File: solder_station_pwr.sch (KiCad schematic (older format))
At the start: 47 parts, among them J1 PWR_MAIN_LINE, J2 FB, J3 Conn_01x04, J5 DESOLDER, J6 Conn_01x03, Q3 2SD669, T1 RingTrafo_40U, T2 220V-7V5, U1 TLC555, U2 L7805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

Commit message: add darligton stage instead of simple transitor
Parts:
- removed Q3: 2SD669, Package_TO_SOT_THT:TO-126-3_Vertical, symbol Device:Q_NPN_EBC
- added Q1: 2N7002, Package_TO_SOT_SMD:SOT-23_Handsoldering, symbol Device:Q_NMOS_GSD
- added Q3: 2SD669, Package_TO_SOT_THT:TO-126-3_Vertical, symbol Device:Q_NPN_ECB
- C14: value 10n -> 4n7
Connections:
- net labels removed: 7V5P
- wire segments 171 -> 176
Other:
- moved on the sheet: D2, J2, J3, J6, T1
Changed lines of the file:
@@
 EESchema Schematic File Version 4
 LIBS:solder_station_pwr-cache
-EELAYER 26 0
+EELAYER 28 0
 EELAYER END
 $Descr A4 11693 8268
@@
 	8450 3050 8950 3050
 Connection ~ 8950 3050
-Text Label 7550 2250 2    50   ~ 0
-7V5P
 $Comp
 L Regulator_Linear:L7805 U2
@@
 L Device:D_Schottky D2
 U 1 1 5B55017E
-P 4050 6300
-F 0 "D2" H 4050 6200 50  0000 C CNN
-F 1 "SD103BW" H 4050 6400 50  0000 C CNN
-F 2 "Diode_SMD:D_SOD-123" H 4050 6300 50  0001 C CNN
-F 3 "~" H 4050 6300 50  0001 C CNN
-	1    4050 6300
+P 4750 6350
+F 0 "D2" H 4750 6250 50  0000 C CNN
+F 1 "SD103BW" H 4750 6450 50  0000 C CNN
+F 2 "Diode_SMD:D_SOD-123" H 4750 6350 50  0001 C CNN
+F 3 "~" H 4750 6350 50  0001 C CNN
+	1    4750 6350
 	0    1    1    0
-$EndComp
-$Comp
-L Device:Q_NPN_EBC Q3
-U 1 1 5B55037E
-P 3600 6300
-F 0 "Q3" H 3450 6450 50  0000 L CNN
-F 1 "2SD669" V 3800 6150 50  0000 L CNN
-F 2 "Package_TO_SOT_THT:TO-126-3_Vertical" H 3800 6400 50  0001 C CNN
-F 3 "~" H 3600 6300 50  0001 C CNN
-	1    3600 6300
-	1    0    0    -1
 $EndComp
 $Comp
@@
 L Device:Transformer_1P_SS T1
 U 1 1 5B56D747
-P 4100 5450
-F 0 "T1" H 4100 5750 50  0000 C CNN
-F 1 "RingTrafo_40U" H 4100 5150 50  0000 C CNN
-F 2 "custom:Transformer_toroid_v_18mm" H 4100 5450 50  0001 C CNN
-F 3 "~" H 4100 5450 50  0001 C CNN
-	1    4100 5450
+P 4800 5450
+F 0 "T1" H 4800 5750 50  0000 C CNN
+F 1 "RingTrafo_40U" H 4800 5150 50  0000 C CNN
+F 2 "custom:Transformer_toroid_v_18mm" H 4800 5450 50  0001 C CNN
+F 3 "~" H 4800 5450 50  0001 C CNN
+	1    4800 5450
 	1    0    0    -1
 $EndComp
@@
 P 1400 6850
 F 0 "C14" H 1515 6896 50  0000 L CNN
-F 1 "10n" H 1515 6805 50  0000 L CNN
+F 1 "4n7" H 1515 6805 50  0000 L CNN
 F 2 "Capacitor_SMD:C_0805_2012Metric_Pad1.15x1.40mm_HandSolder" H 1438 6700 50  0001 C CNN
 F 3 "~" H 1400 6850 50  0001 C CNN
@@
 	3000 6300 2850 6300
 Wire Wire Line
-	3200 6300 3400 6300
-Wire Wire Line
-	3700 6500 3700 6600
-Wire Wire Line
-	3700 7150 2950 7150
-Connection ~ 2950 7150
-Wire Wire Line
-	3700 6600 4050 6600
-Wire Wire Line
-	4050 6600 4050 6450
-Connection ~ 3700 6600
-Wire Wire Line
-	3700 6600 3700 7150
-Wire Wire Line
-	4050 6150 4050 5950
-Wire Wire Line
-	4050 5950 3700 5950
-Wire Wire Line
-	3700 5950 3700 6100
-Wire Wire Line
-	3700 5650 3700 5950
-Connection ~ 3700 5950
-Wire Wire Line
-	3700 5250 3700 5050
-Wire Wire Line
-	3700 5050 2350 5050
+	4400 6750 4400 6850
+Wire Wire Line
+	4400 6850 4750 6850
+Connection ~ 4400 6850
+Wire Wire Line
+	4400 6850 4400 7150
+Wire Wire Line
+	4400 5250 4400 5050
 Connection ~ 2350 5050
 Wire Wire Line
 	2350 5050 2350 4750
-Connection ~ 3700 5050
 Wire Wire Line
 	1400 5650 1400 5050
@@
 	1400 6100 1850 6100
 Wire Wire Line
-	1400 5050 2350 5050
-Wire Wire Line
 	1400 6400 1850 6400
 Wire Wire Line
@@
 Wire Wire Line
 	3350 5800 3350 5950
-Text Label 5150 5550 0    50   ~ 0
-7V5P
-$Comp
-L Connector_Generic:Conn_01x03 J6
-U 1 1 5B54609A
-P 5600 5450
-F 0 "J6" H 5680 5492 50  0000 L CNN
-F 1 "Conn_01x03" H 5680 5401 50  0000 L CNN
-F 2 "Connector_PinSocket_2.54mm:PinSocket_1x03_P2.54mm_Vertical" H 5600 5450 50  0001 C CNN
-F 3 "~" H 5600 5450 50  0001 C CNN
-	1    5600 5450
-	1    0    0    -1
-$EndComp
-Wire Wire Line
-	5400 5550 5150 5550
-Wire Wire Line
-	5150 5350 5400 5350
 $Comp
 L power:+36V #PWR01
 U 1 1 5B5C145A
-P 4950 6850
-F 0 "#PWR01" H 4950 6700 50  0001 C CNN
-F 1 "+36V" H 4965 7023 50  0000 C CNN
-F 2 "" H 4950 6850 50  0001 C CNN
-F 3 "" H 4950 6850 50  0001 C CNN
-	1    4950 6850
+P 5950 6750
+F 0 "#PWR01" H 5950 6600 50  0001 C CNN
+F 1 "+36V" H 5965 6923 50  0000 C CNN
+F 2 "" H 5950 6750 50  0001 C CNN
+F 3 "" H 5950 6750 50  0001 C CNN
+	1    5950 6750
 	1    0    0    -1
 $EndComp
@@
 Text Label 1850 1500 0    50   ~ 0
 UNR_5V
-$Comp
-L Connector_Generic:Conn_01x02 J2
-U 1 1 5B60DB5B
-P 5200 6350
-F 0 "J2" H 5280 6342 50  0000 L CNN
-F 1 "FB" H 5280 6251 50  0000 L CNN
-F 2 "Connector_PinHeader_2.54mm:PinHeader_1x02_P2.54mm_Vertical" H 5200 6350 50  0001 C CNN
-F 3 "~" H 5200 6350 50  0001 C CNN
-	1    5200 6350
-	1    0    0    -1
-$EndComp
-Text Label 4850 5650 2    50   ~ 0
+Text Label 5250 5650 0    50   ~ 0
 FB1
-Text Label 4700 6450 0    50   ~ 0
-FB1
-Wire Wire Line
-	4700 6450 5000 6450
-Wire Wire Line
-	5000 6350 4700 6350
-Text Label 4850 5250 2    50   ~ 0
+Text Label 5250 5250 0    50   ~ 0
 FB2
-Text Label 4700 6350 0    50   ~ 0
-FB2
-Wire Wire Line
-	4500 5450 5400 5450
-Wire Wire Line
-	5150 5050 5150 5350
-Wire Wire Line
-	3700 5050 5150 5050
-Wire Wire Line
-	4850 5650 4500 5650
-Wire Wire Line
-	4500 5250 4850 5250
+Wire Wire Line
+	5200 5250 5550 5250
 $Comp
 L power:+5V #PWR0104
 U 1 1 5B64B6CC
-P 4750 6850
-F 0 "#PWR0104" H 4750 6700 50  0001 C CNN
-F 1 "+5V" H 4765 7023 50  0000 C CNN
-F 2 "" H 4750 6850 50  0001 C CNN
-F 3 "" H 4750 6850 50  0001 C CNN
-	1    4750 6850
+P 5750 6750
+F 0 "#PWR0104" H 5750 6600 50  0001 C CNN
+F 1 "+5V" H 5765 6923 50  0000 C CNN
+F 2 "" H 5750 6750 50  0001 C CNN
+F 3 "" H 5750 6750 50  0001 C CNN
+	1    5750 6750
 	1    0    0    -1
 $EndComp
@@
 L power:-5V #PWR0105
 U 1 1 5B64B913
-P 4750 7500
-F 0 "#PWR0105" H 4750 7600 50  0001 C CNN
-F 1 "-5V" H 4765 7673 50  0000 C CNN
-F 2 "" H 4750 7500 50  0001 C CNN
-F 3 "" H 4750 7500 50  0001 C CNN
-	1    4750 7500
+P 5750 7400
+F 0 "#PWR0105" H 5750 7500 50  0001 C CNN
+F 1 "-5V" H 5765 7573 50  0000 C CNN
+F 2 "" H 5750 7400 50  0001 C CNN
+F 3 "" H 5750 7400 50  0001 C CNN
+	1    5750 7400
 	-1   0    0    1
 $EndComp
@@
 L power:GND #PWR0106
 U 1 1 5B64BA52
-P 4500 7500
-F 0 "#PWR0106" H 4500 7250 50  0001 C CNN
-F 1 "GND" H 4505 7327 50  0000 C CNN
-F 2 "" H 4500 7500 50  0001 C CNN
-F 3 "" H 4500 7500 50  0001 C CNN
-	1    4500 7500
-	1    0    0    -1
-$EndComp
-Wire Wire Line
-	4500 7500 4500 7100
-Wire Wire Line
-	4500 7100 5000 7100
-Wire Wire Line
-	4750 6850 4750 7000
-Wire Wire Line
-	4750 7000 5000 7000
-Wire Wire Line
-	5000 7200 4750 7200
-Wire Wire Line
-	4750 7200 4750 7500
+P 5500 7400
+F 0 "#PWR0106" H 5500 7150 50  0001 C CNN
+F 1 "GND" H 5505 7227 50  0000 C CNN
+F 2 "" H 5500 7400 50  0001 C CNN
+F 3 "" H 5500 7400 50  0001 C CNN
+	1    5500 7400
+	1    0    0    -1
+$EndComp
+Wire Wire Line
+	5500 7400 5500 7000
+Wire Wire Line
+	5500 7000 6000 7000
+Wire Wire Line
+	5750 6750 5750 6900
+Wire Wire Line
+	5750 6900 6000 6900
+Wire Wire Line
+	6000 7100 5750 7100
+Wire Wire Line
+	5750 7100 5750 7400
 $Comp
 L Connector_Generic:Conn_01x04 J3
 U 1 1 5B66CCE5
-P 5200 7100
-F 0 "J3" H 5280 7092 50  0000 L CNN
-F 1 "Conn_01x04" H 5280 7001 50  0000 L CNN
-F 2 "Connector_PinSocket_2.54mm:PinSocket_1x04_P2.54mm_Vertical" H 5200 7100 50  0001 C CNN
-F 3 "~" H 5200 7100 50  0001 C CNN
-	1    5200 7100
-	1    0    0    -1
-$EndComp
-Wire Wire Line
-	4950 6850 4950 7300
-Wire Wire Line
-	4950 7300 5000 7300
+P 6200 7000
+F 0 "J3" H 6280 6992 50  0000 L CNN
+F 1 "Conn_01x04" H 6280 6901 50  0000 L CNN
+F 2 "Connector_PinSocket_2.54mm:PinSocket_1x04_P2.54mm_Vertical" H 6200 7000 50  0001 C CNN
+F 3 "~" H 6200 7000 50  0001 C CNN
+	1    6200 7000
+	1    0    0    -1
+$EndComp
+Wire Wire Line
+	5950 6750 5950 7200
+Wire Wire Line
+	5950 7200 6000 7200
 $Comp
 L power:+36V #PWR0107
@@
 	1300 850  1300 1250
 Connection ~ 1300 1250
+$Comp
+L Device:Q_NPN_ECB Q3
+U 1 1 5BC3B0FA
+P 4300 6550
+F 0 "Q3" H 4250 6700 50  0000 L CNN
+F 1 "2SD669" H 4100 6350 50  0000 L CNN
+F 2 "Package_TO_SOT_THT:TO-126-3_Vertical" H 4500 6650 50  0001 C CNN
+F 3 "~" H 4300 6550 50  0001 C CNN
+	1    4300 6550
+	1    0    0    -1
+$EndComp
+$Comp
+L Device:Q_NMOS_GSD Q1
+U 1 1 5BC54008
+P 3800 6300
+F 0 "Q1" H 4006 6346 50  0000 L CNN
+F 1 "2N7002" H 4006 6255 50  0000 L CNN
+F 2 "Package_TO_SOT_SMD:SOT-23_Handsoldering" H 4000 6400 50  0001 C CNN
+F 3 "~" H 3800 6300 50  0001 C CNN
+	1    3800 6300
+	1    0    0    -1
+$EndComp
+Wire Wire Line
+	5200 5450 5450 5450
+Wire Wire Line
+	3200 6300 3600 6300
+Wire Wire Line
+	4400 5900 3900 5900
+Wire Wire Line
+	3900 5900 3900 6100
+Wire Wire Line
+	4400 5900 4750 5900
+Connection ~ 4400 5900
+Wire Wire Line
+	4750 5900 4750 6200
+Wire Wire Line
+	4400 5900 4400 6350
+Wire Wire Line
+	4750 6500 4750 6850
+Wire Wire Line
+	2950 7150 4400 7150
+Connection ~ 2950 7150
+Wire Wire Line
+	4100 6550 3900 6550
+Wire Wire Line
+	3900 6550 3900 6500
+Wire Wire Line
+	2350 5050 1400 5050
+Wire Wire Line
+	4400 5900 4400 5650
+$Comp
+L Connector_Generic:Conn_01x02 J2
+U 1 1 5B60DB5B
+P 5850 5550
+F 0 "J2" H 5930 5542 50  0000 L CNN
+F 1 "FB" H 5930 5451 50  0000 L CNN
+F 2 "Connector_PinHeader_2.54mm:PinHeader_1x02_P2.54mm_Vertical" H 5850 5550 50  0001 C CNN
+F 3 "~" H 5850 5550 50  0001 C CNN
+	1    5850 5550
+	1    0    0    -1
+$EndComp
+Wire Wire Line
+	4400 5050 5450 5050
+$Comp
+L Connector_Generic:Conn_01x03 J6
+U 1 1 5B54609A
+P 3550 5050
+F 0 "J6" H 3630 5092 50  0000 L CNN
+F 1 "Conn_01x03" H 3630 5001 50  0000 L CNN
+F 2 "Connector_PinSocket_2.54mm:PinSocket_1x03_P2.54mm_Vertical" H 3550 5050 50  0001 C CNN
+F 3 "~" H 3550 5050 50  0001 C CNN
+	1    3550 5050
+	-1   0    0    -1
+$EndComp
+Wire Wire Line
+	5450 5450 5450 5050
+Wire Wire Line
+	5200 5650 5650 5650
+Wire Wire Line
+	5550 5250 5550 5550
+Wire Wire Line
+	5550 5550 5650 5550
+$Comp
+L power:+5V #PWR02
+U 1 1 5BE33567
+P 4400 4700
+F 0 "#PWR02" H 4400 4550 50  0001 C CNN
+F 1 "+5V" H 4415 4873 50  0000 C CNN
+F 2 "" H 4400 4700 50  0001 C CNN
+F 3 "" H 4400 4700 50  0001 C CNN
+	1    4400 4700
+	-1   0    0    -1
+$EndComp
+Wire Wire Line
+	4400 4700 4400 4950
+Text Label 4100 5150 2    50   ~ 0
+UNR_5V
+Wire Wire Line
+	3750 5150 4100 5150
+Wire Wire Line
+	3750 5050 4400 5050
+Connection ~ 4400 5050
+Wire Wire Line
+	3750 4950 4400 4950
 $EndSCHEMATC

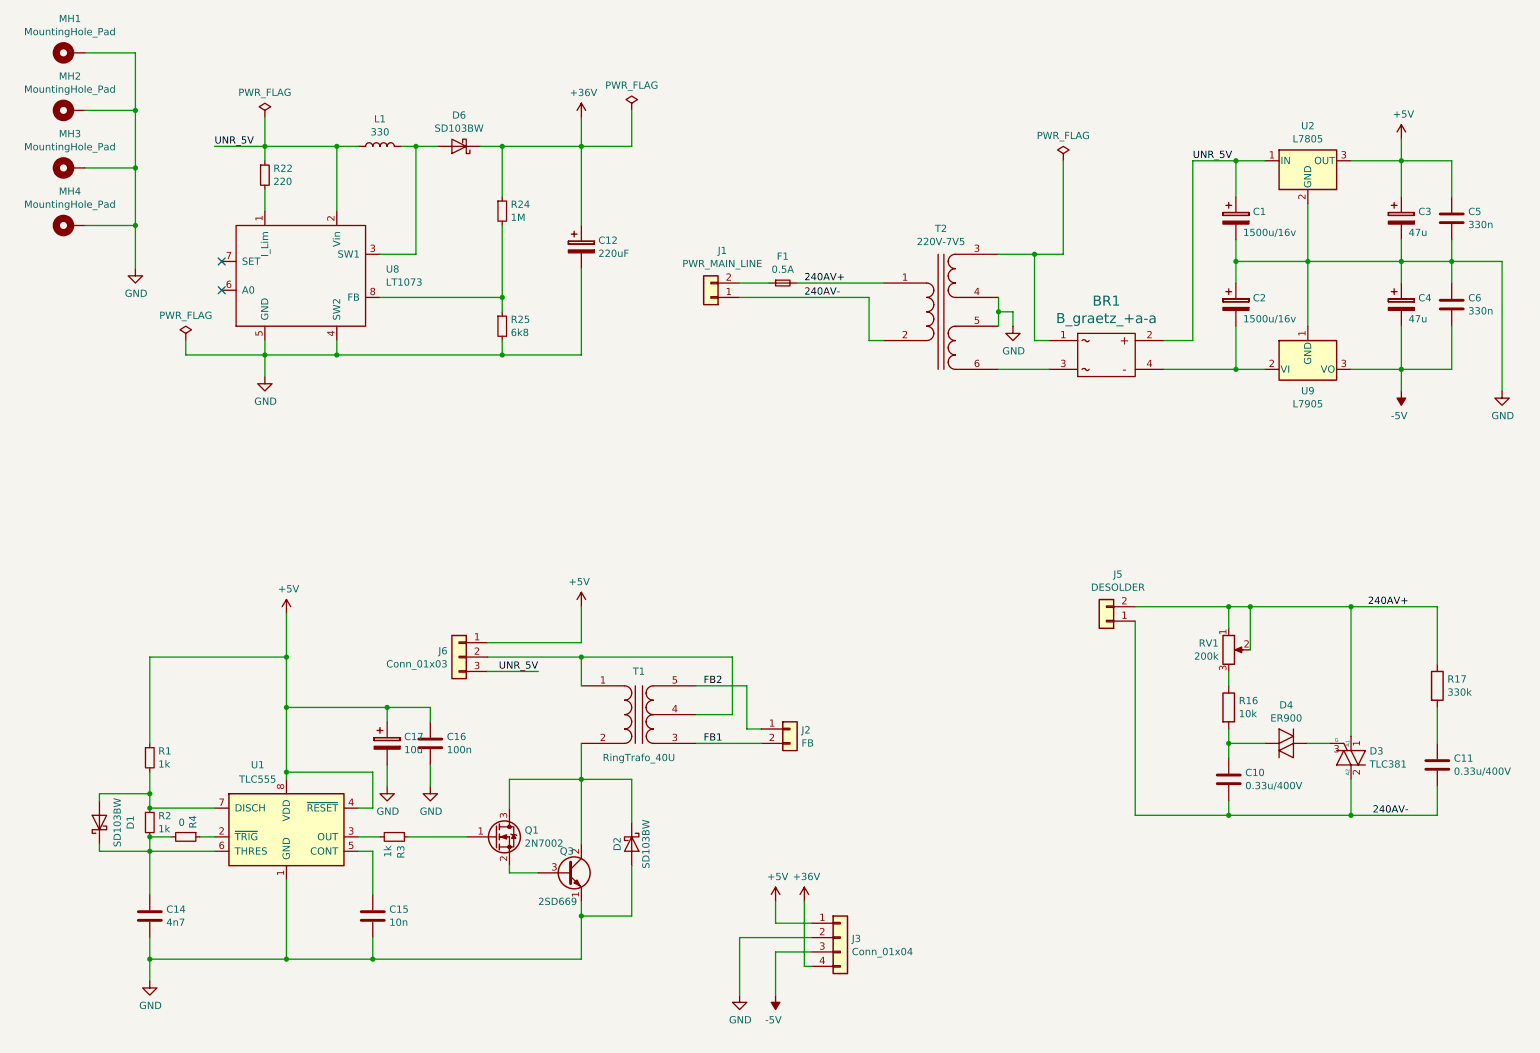
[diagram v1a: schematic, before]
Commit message: remove ne555, using the atmega pwm OC0B to control the transistor
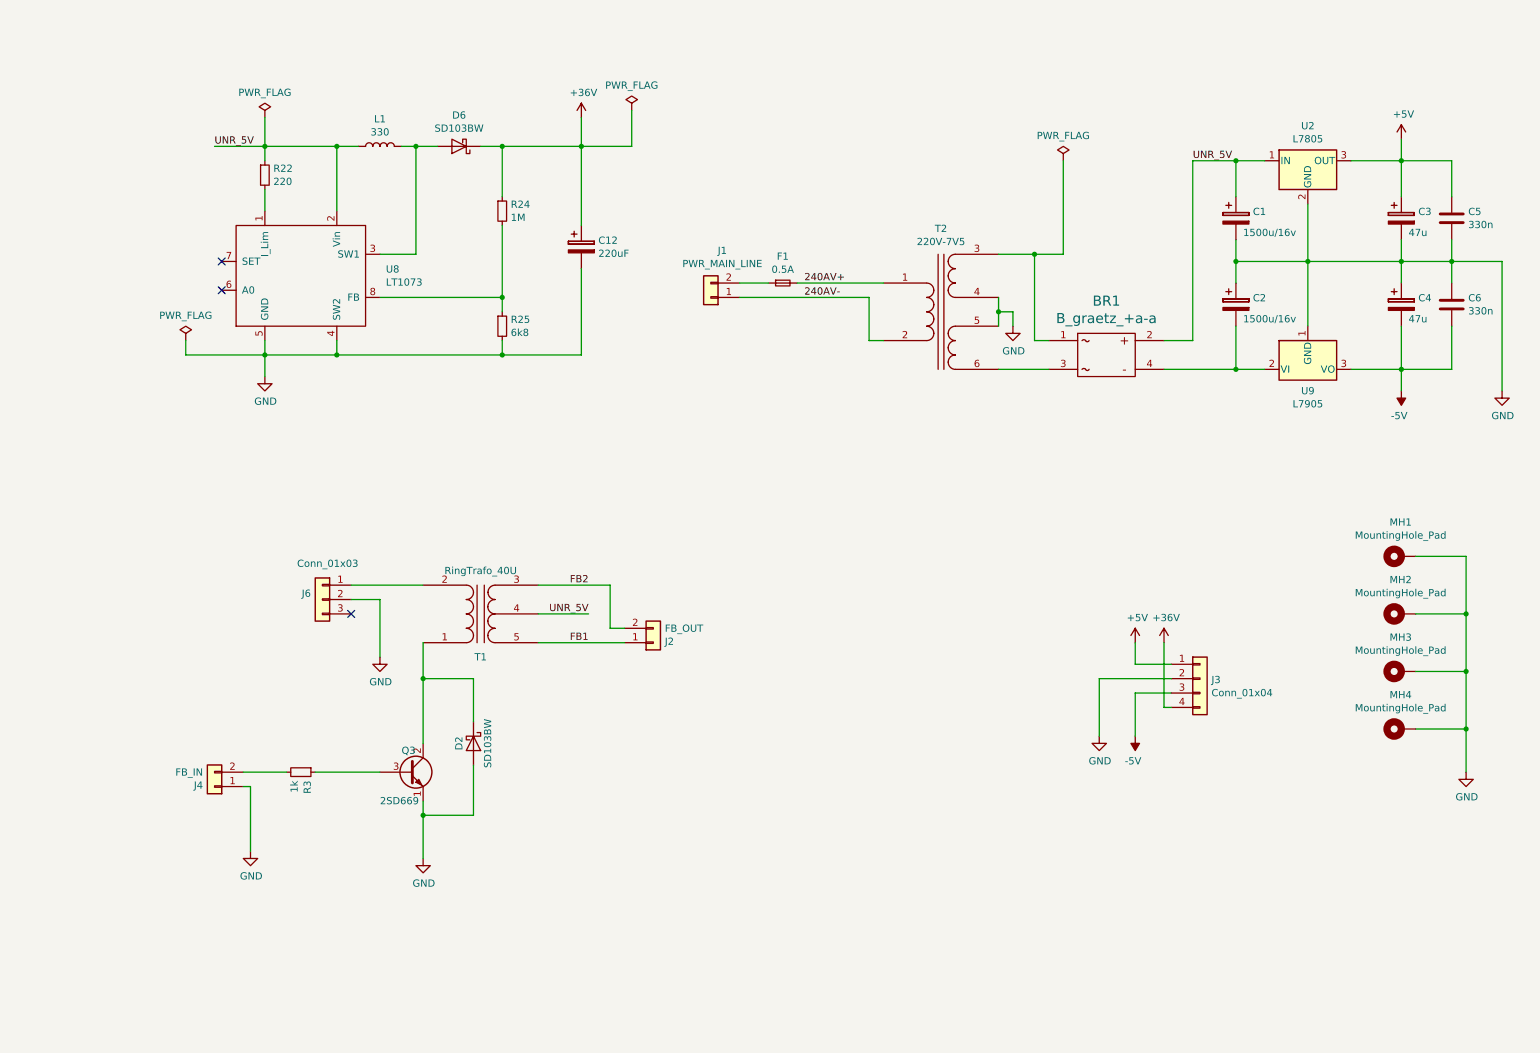
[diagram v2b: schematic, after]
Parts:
- removed C10, C11: 0.33u/400V, Capacitor_THT:C_Rect_L19.0mm_W8.0mm_P15.00mm_MKS4, symbol Device:C
- removed C14: 4n7, Capacitor_SMD:C_0805_2012Metric_Pad1.15x1.40mm_HandSolder, symbol Device:C
- removed C15: 10n, Capacitor_SMD:C_0805_2012Metric_Pad1.15x1.40mm_HandSolder, symbol Device:C
- removed C16: 100n, Capacitor_SMD:C_0805_2012Metric_Pad1.15x1.40mm_HandSolder, symbol Device:C
- removed C17: 10u, Capacitor_Tantalum_SMD:CP_EIA-6032-15_Kemet-U_Pad2.25x2.35mm_HandSolder, symbol Device:CP
- removed D1: SD103BW, Diode_SMD:D_SOD-123, symbol Device:D_Schottky
- removed D3: TLC381, Package_TO_SOT_THT:TO-220-3_Vertical, symbol Device:Q_TRIAC_A1A2G
- removed D4: ER900, Diode_THT:D_A-405_P7.62mm_Horizontal, symbol Device:DIAC
- removed J5: DESOLDER, Connector_Wire:SolderWirePad_1x02_P5.08mm_Drill1.5mm, symbol Connector_Generic:Conn_01x02
- removed Q1: 2N7002, Package_TO_SOT_SMD:SOT-23_Handsoldering, symbol Device:Q_NMOS_GSD
- removed R1, R2: 1k, Resistor_SMD:R_0805_2012Metric_Pad1.15x1.40mm_HandSolder, symbol Device:R_Small
- removed R16: 10k, Resistor_THT:R_Axial_DIN0207_L6.3mm_D2.5mm_P10.16mm_Horizontal, symbol Device:R
- removed R17: 330k, Resistor_THT:R_Axial_DIN0207_L6.3mm_D2.5mm_P10.16mm_Horizontal, symbol Device:R
- removed R4: 0, Resistor_SMD:R_1206_3216Metric_Pad1.42x1.75mm_HandSolder, symbol Device:R_Small
- removed RV1: 200k, TerminalBlock_4Ucon:TerminalBlock_4Ucon_1x03_P3.50mm_Horizontal, symbol Device:R_POT
- removed U1: TLC555, Package_SO:SOIC-8_3.9x4.9mm_P1.27mm, symbol Timer:TLC555
- added J4: FB_IN, Connector_PinHeader_2.54mm:PinHeader_1x02_P2.54mm_Vertical, symbol Connector_Generic:Conn_01x02
- J2: value FB -> FB_OUT
- J6: footprint Connector_PinSocket_2.54mm:PinSocket_1x03_P2.54mm_Vertical -> Connector_PinSocket_2.54mm:PinSocket_1x03_P2.54mm_Vertical_SMD_Pin1Left
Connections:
- net +5V: no longer J6.1 (Pin_1)
- net FB1: now also J2.1 (Pin_1), T1.5 (SB); no longer J2.2 (Pin_2), T1.3 (SA)
- net FB2: now also J2.2 (Pin_2), T1.3 (SA); no longer J2.1 (Pin_1), T1.5 (SB)
- net GND: now also J6.2 (Pin_2), J4.1 (Pin_1)
- net UNR_5V: now also T1.4 (SC); no longer J6.3 (Pin_3)
- net at R3.2: now also J4.2 (Pin_2)
- net at D2.1 (K), Q3.2 (C): now also T1.1 (AA); no longer T1.2 (AB)
- net at R3.1: now also Q3.3 (B)
- new net: J6.1 (Pin_1), T1.2 (AB)
- no-connect marks 2 -> 3
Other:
- moved on the sheet: D2, J2, J3, J6, MH1, MH2, MH3, MH4, Q3, R3, T1

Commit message: Add power suppply has now just 2 differents 5 volt and a -5 volt
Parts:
- removed D2: SD103BW, Diode_SMD:D_SOD-123, symbol Device:D_Schottky
- removed J4: FB_IN, Connector_PinHeader_2.54mm:PinHeader_1x02_P2.54mm_Vertical, symbol Connector_Generic:Conn_01x02
- removed J6: Conn_01x03, Connector_PinSocket_2.54mm:PinSocket_1x03_P2.54mm_Vertical_SMD_Pin1Left, symbol Connector_Generic:Conn_01x03
- removed Q3: 2SD669, Package_TO_SOT_THT:TO-126-3_Vertical, symbol Device:Q_NPN_ECB
- removed R3: 1k, Resistor_SMD:R_0805_2012Metric_Pad1.15x1.40mm_HandSolder, symbol Device:R_Small
- removed T1: RingTrafo_40U, custom:Transformer_toroid_v_18mm, symbol Device:Transformer_1P_SS
- added R1, R2: 0, Resistor_SMD:R_1206_3216Metric_Pad1.42x1.75mm_HandSolder, symbol Device:R_Small
- BR1: symbol custom:BRIGE_RECTIFIER_+a-a -> solder_station_pwr-rescue:BRIGE_RECTIFIER_+a-a-custom
- J2: value FB_OUT -> PWR_HV; footprint Connector_PinHeader_2.54mm:PinHeader_1x02_P2.54mm_Vertical -> Connector_Wire:SolderWirePad_1x02_P5.08mm_Drill1.5mm
- J3: value Conn_01x04 -> PWR_LV
- R24: value 1M -> 560k
- R25: value 6k8 -> 22k
- U8: symbol custom:LT1073 -> solder_station_pwr-rescue:LT1073-custom
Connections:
- net FB2 is gone; now on net GND: J2.2 (Pin_2)
- net +5V: now also J3.2 (Pin_2); no longer J3.1 (Pin_1)
- net -5V: now also J3.4 (Pin_4); no longer J3.3 (Pin_3)
- net GND: now also D6.2 (A), J3.3 (Pin_3); no longer J3.2 (Pin_2), U8.4 (SW2)
- net at C2.2, U9.2 (VI): now also BR1.2, R1.1, R1.2; no longer BR1.4
- net at T2.3 (SA): now also BR1.3; no longer BR1.1
- net at T2.6 (SD): now also BR1.1; no longer BR1.3
- net +36V renamed +5VA
- net +5VA: now also J3.1 (Pin_1), L1.2; no longer D6.1 (K), J3.4 (Pin_4)
- net FB1 renamed +12V
- net +12V: now also R22.1, U8.2 (Vin), U8.3 (SW1)
- removed net UNR_5V: BR1.2, C1.1, L1.1, R22.1, U2.1 (IN), U8.2 (Vin)
- new net: D6.1 (K), L1.1, U8.4 (SW2)
- new net: BR1.4, C1.1, R2.1, R2.2, U2.1 (IN)
- no-connect marks 3 -> 2
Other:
- moved on the sheet: BR1, C1, C12, C2, C3, C4, C5, C6, D6, F1, J1, J3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
